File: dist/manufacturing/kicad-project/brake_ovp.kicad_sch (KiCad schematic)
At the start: 13 parts, among them J3 B2P-VH(LF)(SN), Q16 CSD19534Q5A, U14 TLV3201AIDBVR, U15 UCC27511DBVR

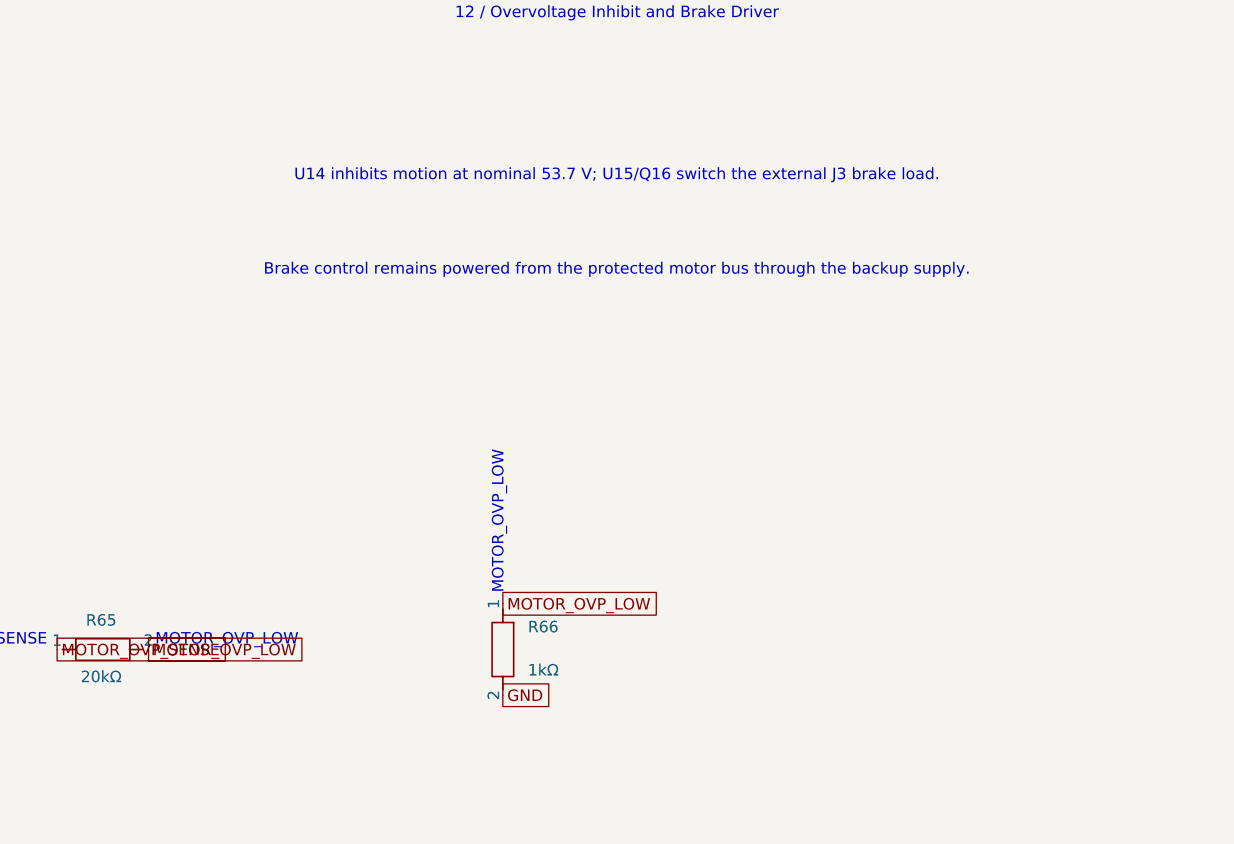
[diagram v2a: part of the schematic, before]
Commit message: Refine protection limits and restore native component references
Restore footprint-native reference labels, including SW1/SW2, and retain
source, assembly and external-equipment review updates.

Apply TPS26630 with R25 4.99k, R61 16.2k and R66 1.2k to source and native
CAD. Retain the restricted current ceiling and motion/configuration locks.
Record threshold tolerances, thirteen behavioral simulation cases, source
hashes and native geometry-equivalence evidence.

Validation: source/assembly builds, typecheck, 27 design tests, 14 power
checks and firmware host tests pass. Native ERC and unconnected/parity
counts are zero. Full review fails the stock gate; 403 silkscreen/text
findings, brake-fault protection and hardware qualification remain open.
Viewer/manufacturing archives are historical for the protection changes.
Preserve raw tool logs including their emitted trailing whitespace.

Keep this engineering branch separate from origin/main 4836266, which
independently changes brake feedback, routing and protection values.
No powered operation or fabrication release is authorized.
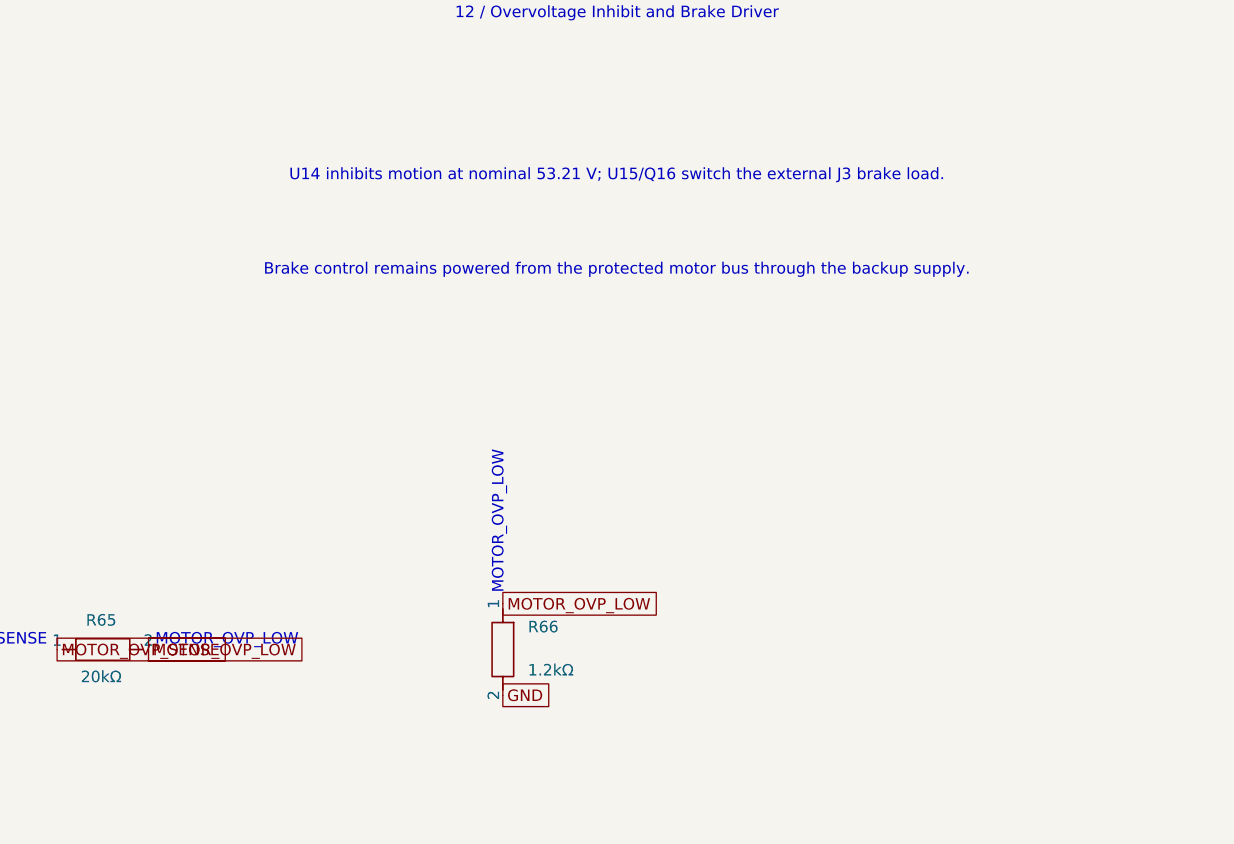
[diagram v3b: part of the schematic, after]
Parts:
- R66: value 1kΩ -> 1.2kΩ
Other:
- note added: "U14 inhibits motion at nominal 53.21 V; U15/Q16 switch the external J3 brake load."
- note removed: "U14 inhibits motion at nominal 53.7 V; U15/Q16 switch the external J3 brake load."
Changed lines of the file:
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@@
       )
     )
-    (property "Value" "1kΩ"
+    (property "Value" "1.2kΩ"
       (id 1)
       (at 305.03249999999997 128.025 0)
@@
     )
   )
-  (text "U14 inhibits motion at nominal 53.7 V; U15/Q16 switch the external J3 brake load."
+  (text "U14 inhibits motion at nominal 53.21 V; U15/Q16 switch the external J3 brake load."
     (at 314.9325 73.125 0)
     (effects
